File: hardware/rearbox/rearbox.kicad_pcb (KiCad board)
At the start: 4 copper layers, 80 x 60 mm, 218 parts, among them IC2 TPS54202HDDCR, J1 STDC14, J2 ST-LINK, J3 Conn_02x28_Top_Bottom, J4 Auxiliary, J5 XIAO ESP32S3 Sense, Q1 BUK6D210, Q6 BUK6D210, U1 LM4040C33FTA, U10 TLP291-4, U11 TLP291-4, U12 TLP291-4, U17 MCP6N11T-002, U18 MCP6001, U19 MCP6N11T-002, U2 STM32G473RCTx, U20 MCP6001, U21 MCP6N11T-002, U22 MCP6001, U23 MCP6N11T-002, U24 MCP6001, U4 TLV743P, U9 TCA6416ARTWR, Y1 48MHz

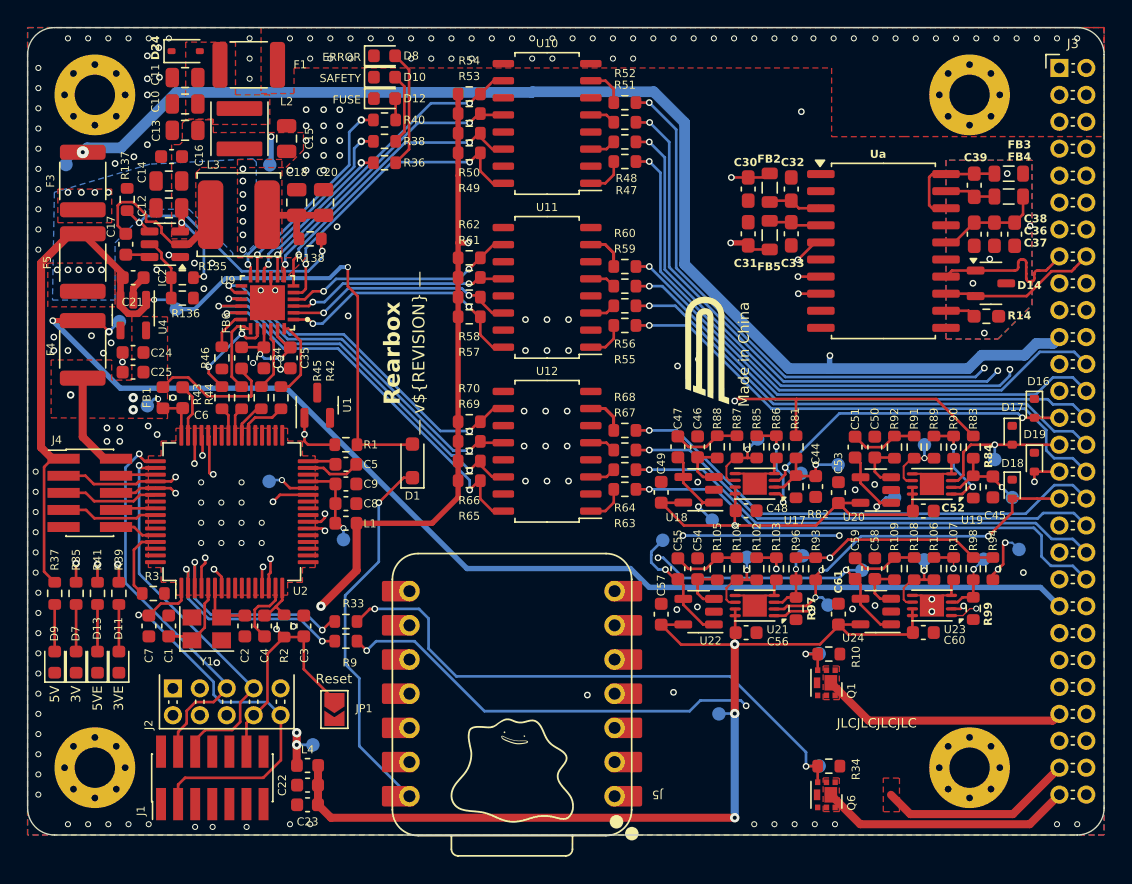
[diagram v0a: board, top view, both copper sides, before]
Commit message: Added an auxillary transistor for rear brakelights in case they burn up again and fixed some GNDISO_CAN problems
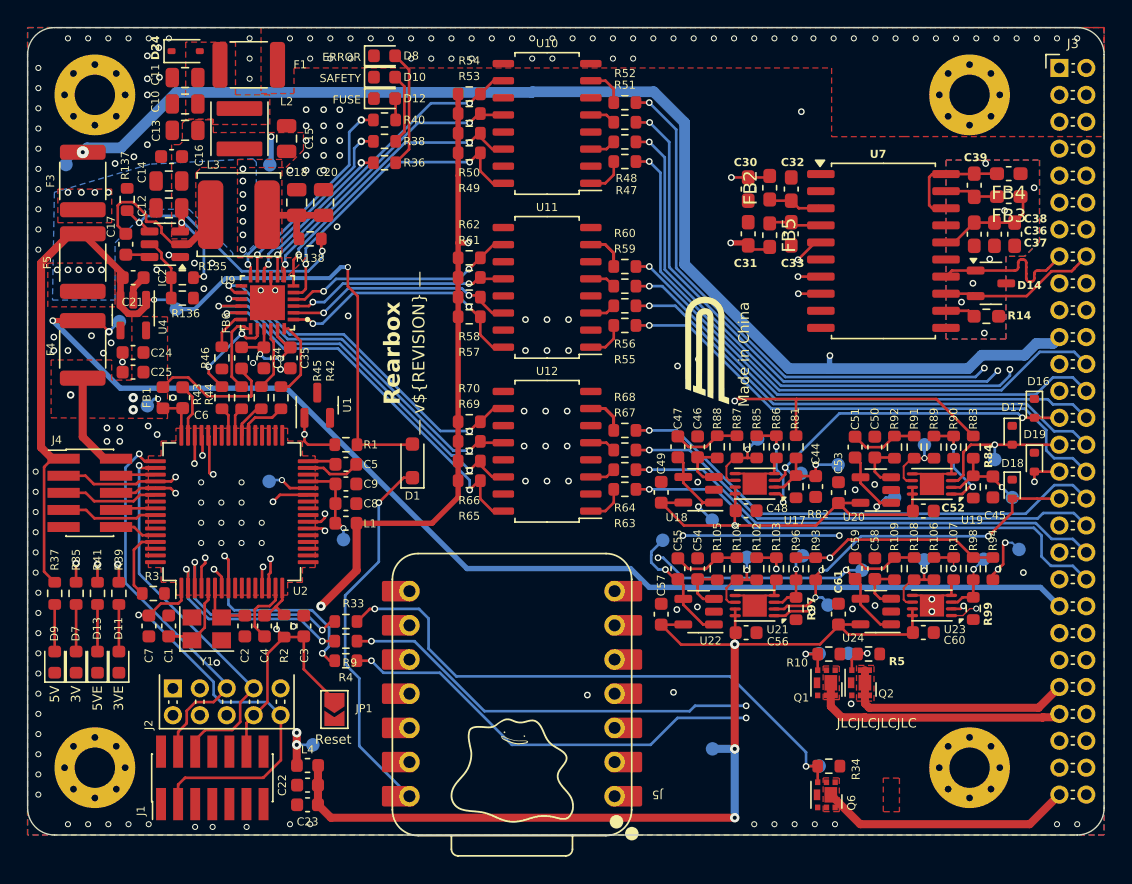
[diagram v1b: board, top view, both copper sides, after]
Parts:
- added Q2: BUK6D210, Local_Library:Diodes_UDFN2020-6_Type-F, F.Cu at (165.9, 122.7)
- added R4: 100R, Resistor_SMD:R_0603_1608Metric, F.Cu at (127.7, 121.0)
- added R5: 10k, Resistor_SMD:R_0603_1608Metric, F.Cu at (166.5, 120.5)
- added TP5: TestPoint_Small, TestPoint:TestPoint_Pad_D1.0mm, B.Cu at (165.0, 120.5)
- FB2, FB3, FB4, FB5: footprint Inductor_SMD:L_0805_2012Metric -> Inductor_SMD:L_0603_1608Metric_Pad1.05x0.95mm_HandSolder
- moved TP10 2.64 mm to (154.9, 127.6)
- renumbered Ua to U7
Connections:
- J3 pad 47: unconnected-(J3-Pin_47-Pad47) -> BACKUP_BRAKE_LIGHT_OUT
- U2 pad 8: unconnected-(U2-PC0-Pad8) -> /BACKUP_BRAKE_LIGHT
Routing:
- net Net-(Q2-G): track 0.00 -> 46.9 mm, vias 0 -> 3
- net /BACKUP_BRAKE_LIGHT: track 0.00 -> 17.7 mm, vias 0 -> 2
- net BACKUP_BRAKE_LIGHT_OUT: track 0.00 -> 17.7 mm
- net unconnected-(J3-Pin_53-Pad53): track 14.5 -> 0.00 mm
- net Net-(Q1-G): track 41.3 -> 40.3 mm
- net BRAKE_LIGHT_OUT: track 18.4 -> 19.2 mm
- net +3.3VA: track 143.5 -> 144.0 mm
- net GND: vias 147 -> 148
- net /CAN Transceivers/CAN Transceiver/GNDISO_CAN: vias 5 -> 7
- added copper zone on F.Cu, net BACKUP_BRAKE_LIGHT_OUT

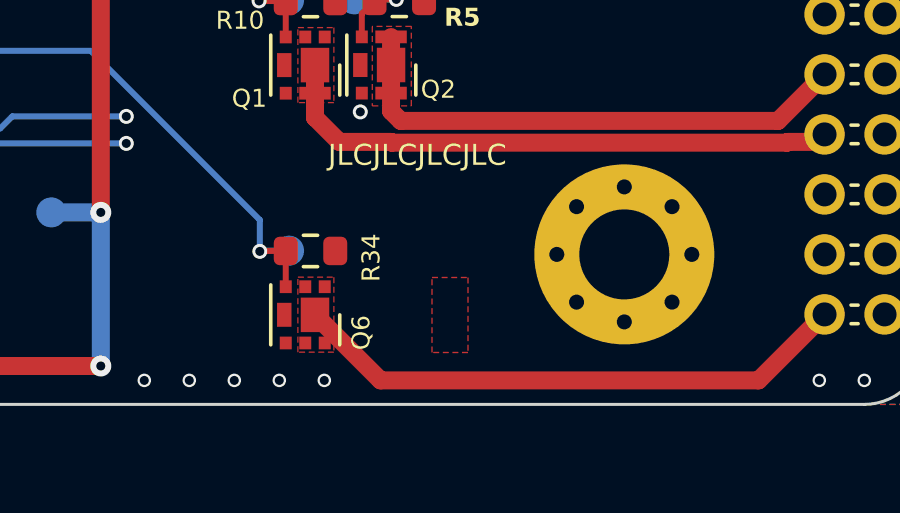
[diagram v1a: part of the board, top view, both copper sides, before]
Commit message: Removed a leftover fill zone
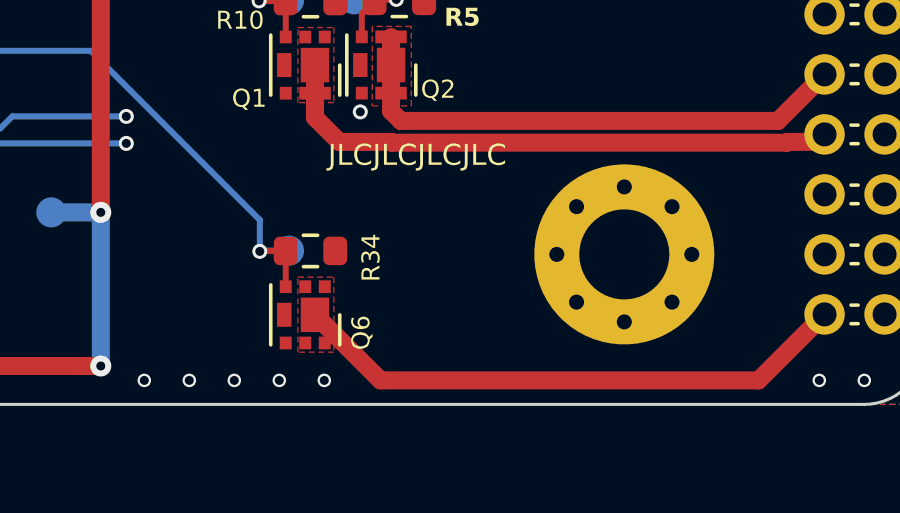
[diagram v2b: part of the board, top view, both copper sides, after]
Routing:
- removed copper zone on F.Cu, net unconnected-(J3-Pin_53-Pad53)
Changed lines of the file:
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@@
-	)
-	(zone
-		(net 37)
-		(net_name "unconnected-(J3-Pin_53-Pad53)")
-		(locked yes)
-		(layer "F.Cu")
-		(hatch edge 0.5)
-		(priority 1)
-		(connect_pads yes
-			(clearance 0.2)
-		)
-		(min_thickness 0.25)
-		(filled_areas_thickness no)
-		(fill yes
-			(thermal_gap 0.15)
-			(thermal_bridge_width 0.5)
-		)
-		(polygon
-			(pts
-				(xy 167.59 129.77) (xy 168.79 129.77) (xy 168.79 132.27) (xy 167.59 132.27)
-			)
-		)
 	)
 	(zone
